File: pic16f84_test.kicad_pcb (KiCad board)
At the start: 2 copper layers, 59.9 x 20.6 mm, 20 parts, among them J1 ICSP, J2 Conn_01x03, Q1 2N7002, Q2 2N7002, Q3 2N7002, Q4 2N7002, U1 PIC16F54-IP

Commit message: done with revision 0.01
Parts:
- added G***: LOGO, custom_logo:pimium_paprika_7mm, F.Cu at (112.0, 97.8)
- added H1: MountingHole, MountingHole:MountingHole_2.2mm_M2, F.Cu at (159.5, 105.7)
- added H2: MountingHole, MountingHole:MountingHole_2.2mm_M2, F.Cu at (94.2, 90.2)
- added H3: MountingHole, MountingHole:MountingHole_2.2mm_M2, F.Cu at (159.5, 90.4)
- added H4: MountingHole, MountingHole:MountingHole_2.2mm_M2, F.Cu at (94.2, 105.7)
- turned R7 to 90 degrees
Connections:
- AFF1 pad 10: /SEG_G -> /PGD
- AFF1 pad 9: /SEG_F -> /PGC
- AFF2 pad 10: /SEG_G -> /PGD
- AFF2 pad 9: /SEG_F -> /PGC
- AFF3 pad 10: /SEG_G -> /PGD
- AFF3 pad 9: /SEG_F -> /PGC
- AFF4 pad 10: /SEG_G -> /PGD
- AFF4 pad 9: /SEG_F -> /PGC
- J1 pad 4: (no net) -> /PGC
- J1 pad 5: (no net) -> /PGD
- U1 pad 12: /SEG_F -> /PGC
- U1 pad 13: /SEG_G -> /PGD
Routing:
- net GND: track 0.00 -> 112.1 mm
- net /PGD: track 0.00 -> 107.8 mm
- net /PGC: track 0.00 -> 107.1 mm
- net /SEG_C: track 0.00 -> 93.0 mm
- net Net-(J1-Pad1): track 0.00 -> 68.8 mm
- net VCC: track 0.00 -> 65.7 mm
- net /SEG_D: track 0.00 -> 60.5 mm
- net /SEG_A: track 0.00 -> 56.5 mm
- net /SEG_B: track 0.00 -> 54.0 mm
- net /SEG_E: track 0.00 -> 53.9 mm
- net /DIO: track 0.00 -> 35.7 mm, vias 0 -> 1
- net /DIG_0: track 0.00 -> 25.0 mm, vias 0 -> 1
- net /DIG_3: track 0.00 -> 23.7 mm, vias 0 -> 1
- net /DIG_2: track 0.00 -> 11.8 mm, vias 0 -> 1
- net Net-(C4-Pad1): track 0.00 -> 11.2 mm
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- added copper zone on B.Cu, net GND
- added copper zone on F.Cu, net GND
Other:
- board size 59.9 x 20.6 mm -> 70.4 x 20.6 mm
- board text added: "PIC16F54 7 SEGMENTS v0.0.1"

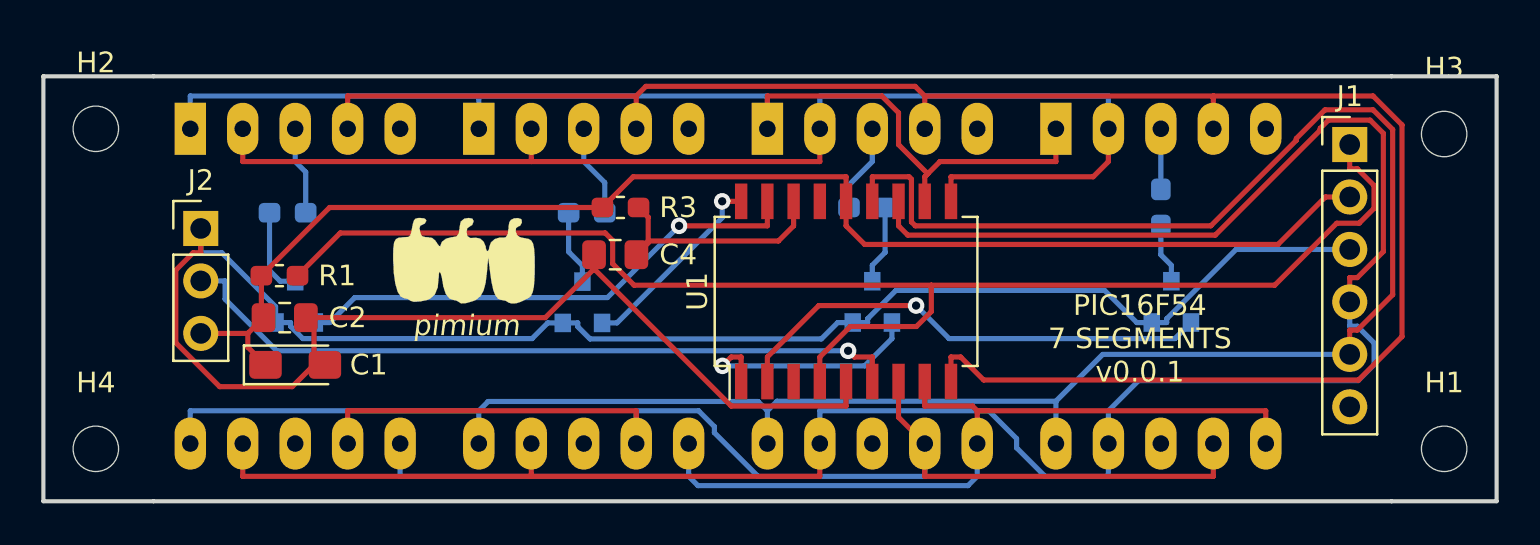
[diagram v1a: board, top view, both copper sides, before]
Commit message: augment the diameter of the mounting holes
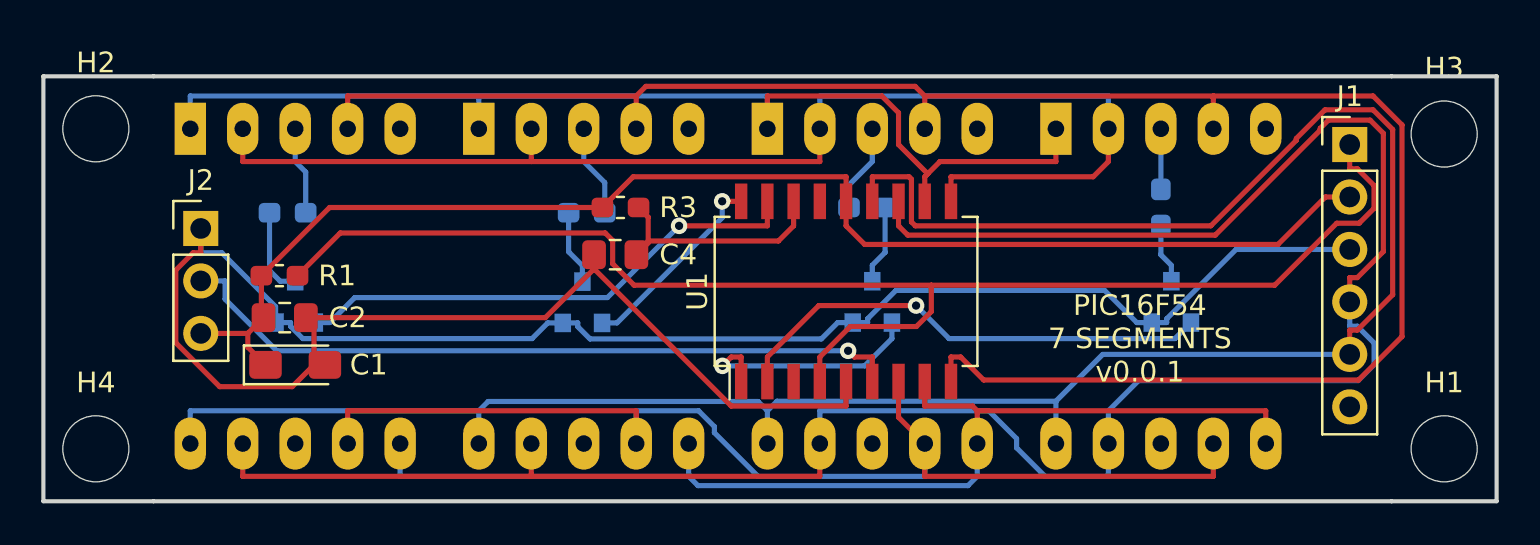
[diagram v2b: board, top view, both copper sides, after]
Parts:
- removed G***: LOGO, custom_logo:pimium_paprika_7mm
- H1, H2, H3, H4: footprint MountingHole:MountingHole_2.2mm_M2 -> modules:MountingHole_3.2mm_M2

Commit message: just 3 segments
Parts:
- removed AFF4: LTS-6980HR, Display_7Segment:7SegmentLED_LTS6760_LTS6780
- removed Q4: 2N7002, Package_TO_SOT_SMD:SOT-23
- added J3: Conn_01x03, Connector_PinHeader_2.54mm:PinHeader_1x03_P2.54mm_Vertical, F.Cu at (144.5, 95.5)
- added R10: 100, Resistor_SMD:R_0603_1608Metric_Pad1.05x0.95mm_HandSolder, F.Cu at (136.9, 94.7)
- added R2: 100, Resistor_SMD:R_0603_1608Metric_Pad1.05x0.95mm_HandSolder, F.Cu at (126.7, 94.6)
- added R8: 100, Resistor_SMD:R_0603_1608Metric_Pad1.05x0.95mm_HandSolder, F.Cu at (129.3, 100.8)
- added R9: 100, Resistor_SMD:R_0603_1608Metric_Pad1.05x0.95mm_HandSolder, F.Cu at (126.7, 100.8)
- R4, R5, R6, R7: moved to F.Cu
- moved R3 21.7 mm to (98.4, 98.6)
- moved C4 21.3 mm to (98.6, 100.6), turned to 0 degrees
- moved U1 18.3 mm to (112.3, 97.8)
- moved R4 18.1 mm to (120.4, 100.8), turned to 90 degrees
- moved R7 16.5 mm to (129.3, 94.6), turned to 270 degrees
- moved H1 14.5 mm to (145.0, 105.7)
- moved H3 14.5 mm to (145.0, 90.4)
- moved J1 14.2 mm to (140.7, 90.9)
- moved R5 8.25 mm to (122.9, 100.8), turned to 90 degrees
- moved C2 7.42 mm to (98.8, 93.5)
- moved C1 7.42 mm to (99.3, 95.8)
- moved R1 7.19 mm to (98.3, 102.6)
- moved J2 5.33 mm to (94.0, 95.0)
- moved Q3 4.30 mm to (131.8, 94.2)
- moved Q2 4.08 mm to (117.9, 94.5)
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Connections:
- AFF1 pad 10: /PGD -> /SEG_G
- AFF1 pad 5: (no net) -> /SEG_DP
- AFF1 pad 9: /PGC -> /SEG_F
- AFF2 pad 10: /PGD -> /SEG_G
- AFF2 pad 5: (no net) -> /SEG_DP
- AFF2 pad 9: /PGC -> /SEG_F
- AFF3 pad 10: /PGD -> /SEG_G
- AFF3 pad 5: (no net) -> /SEG_DP
- AFF3 pad 9: /PGC -> /SEG_F
- J1 pad 4: /PGC -> /PGD
- J1 pad 5: /PGD -> /PGC
- Q1 pad 3: Net-(Q1-Pad3) -> Net-(AFF1-Pad3)
- Q2 pad 3: Net-(Q2-Pad3) -> Net-(AFF2-Pad3)
- Q3 pad 3: Net-(Q3-Pad3) -> Net-(AFF3-Pad3)
- R4 pad 1: Net-(Q1-Pad3) -> /SEG_A
- R4 pad 2: Net-(AFF1-Pad3) -> Net-(R4-Pad2)
- R5 pad 1: Net-(Q2-Pad3) -> /SEG_B
- R5 pad 2: Net-(AFF2-Pad3) -> Net-(R5-Pad2)
- R6 pad 1: Net-(Q3-Pad3) -> /SEG_C
- R6 pad 2: Net-(AFF3-Pad3) -> Net-(R6-Pad2)
- R7 pad 1: Net-(Q4-Pad3) -> /SEG_D
- R7 pad 2: Net-(AFF4-Pad3) -> Net-(R7-Pad2)
- U1 pad 10: /SEG_D -> Net-(R2-Pad2)
- U1 pad 11: /SEG_E -> Net-(R8-Pad2)
- U1 pad 2: /DIG_3 -> /DIO
- U1 pad 6: /DIO -> Net-(R4-Pad2)
- U1 pad 7: /SEG_A -> Net-(R5-Pad2)
- U1 pad 8: /SEG_B -> Net-(R6-Pad2)
- U1 pad 9: /SEG_C -> Net-(R7-Pad2)
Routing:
- net /PGC: track 107.1 -> 29.8 mm
- net /PGD: track 107.8 -> 49.9 mm
- net /SEG_C: track 93.0 -> 38.7 mm
- net Net-(R6-Pad2): track 0.00 -> 42.3 mm
- net /SEG_DP: track 0.00 -> 41.0 mm
- net /SEG_G: track 0.00 -> 40.2 mm
- net /SEG_F: track 0.00 -> 38.4 mm
- net GND: track 112.1 -> 81.8 mm, vias 0 -> 1
- net /DIO: track 35.7 -> 64.3 mm
- net VCC: track 65.7 -> 90.3 mm
- net /SEG_D: track 60.5 -> 36.6 mm
- net /DIG_3: track 23.7 -> 0.00 mm, vias 1 -> 0
- net /SEG_A: track 56.5 -> 36.8 mm
- net /DIG_0: track 25.0 -> 5.39 mm
- net /SEG_E: track 53.9 -> 34.7 mm
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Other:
- board size 70.4 x 20.6 mm -> 55.9 x 20.6 mm
- board text added: "VCC DIO GND"
